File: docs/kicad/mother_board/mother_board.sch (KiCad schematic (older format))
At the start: 14 parts, among them J1 EXPR, J2 TFT_CONTROL, J3 TFT_DATA, J4 SERIAL, J5 LEDS, J6 ROTARY12, J7 ROTARY34, J8 SW_OUT, J9 SW_IN, U1 myTeensy3.6

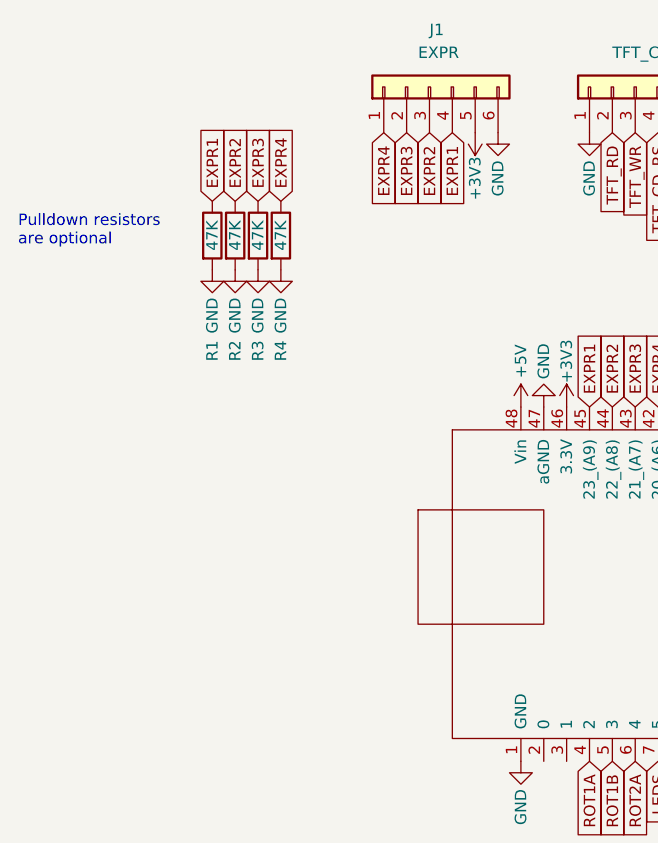
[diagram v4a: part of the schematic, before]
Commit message: added 1K resistor to pedal power to keep from crashing while inserting plugs
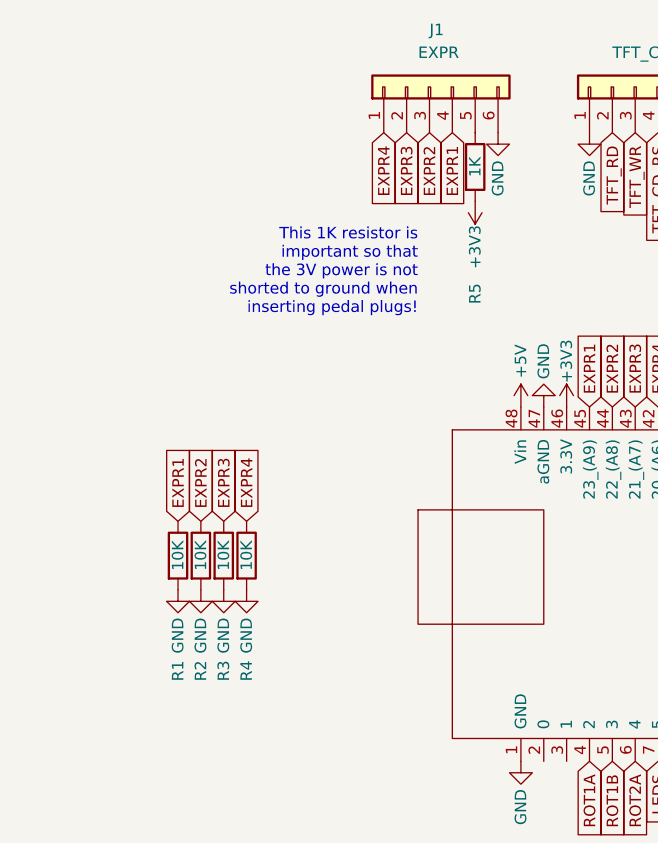
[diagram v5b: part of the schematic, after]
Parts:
- added R5: 1K, 0_my_footprints:myResistor, symbol Device:R
- R1, R2, R3, R4: value 47K -> 10K
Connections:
- net +3V3: now also R5.2; no longer J1.5 (Pin_5)
- new net: J1.5 (Pin_5), R5.1
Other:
- note added: "This 1K resistor is\nimportant so that\nthe 3V power is not \nshorted to ground when \ninserting pedal plugs!\n"
- note removed: "Pulldown resistors\nare optional"
- moved on the sheet: R1, R2, R3, R4
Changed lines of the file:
@@
 L power:+3V3 #PWR06
 U 1 1 64D07CE1
-P 4150 1500
-F 0 "#PWR06" H 4150 1350 50  0001 C CNN
-F 1 "+3V3" V 4150 1700 50  0000 C CNN
-F 2 "" H 4150 1500 50  0001 C CNN
-F 3 "" H 4150 1500 50  0001 C CNN
-	1    4150 1500
+P 4150 1800
+F 0 "#PWR06" H 4150 1650 50  0001 C CNN
+F 1 "+3V3" V 4150 2000 50  0000 C CNN
+F 2 "" H 4150 1800 50  0001 C CNN
+F 3 "" H 4150 1800 50  0001 C CNN
+	1    4150 1800
 	1    0    0    1
 $EndComp
-Text GLabel 3000 1800 1    50   Input ~ 0
+Text GLabel 2850 3200 1    50   Input ~ 0
 EXPR1
-Text GLabel 3100 1800 1    50   Input ~ 0
+Text GLabel 2950 3200 1    50   Input ~ 0
 EXPR2
-Text GLabel 3200 1800 1    50   Input ~ 0
+Text GLabel 3050 3200 1    50   Input ~ 0
 EXPR3
-Text GLabel 3300 1800 1    50   Input ~ 0
+Text GLabel 3150 3200 1    50   Input ~ 0
 EXPR4
 $Comp
 L Device:R R2
 U 1 1 64E4ADF9
-P 3100 1950
-F 0 "R2" V 3100 1400 50  0000 L CNN
-F 1 "47K" V 3100 1950 50  0000 C CNN
-F 2 "0_my_footprints:myResistor" V 3030 1950 50  0001 C CNN
-F 3 "~" H 3100 1950 50  0001 C CNN
-	1    3100 1950
+P 2950 3350
+F 0 "R2" V 2950 2800 50  0000 L CNN
+F 1 "10K" V 2950 3350 50  0000 C CNN
+F 2 "0_my_footprints:myResistor" V 2880 3350 50  0001 C CNN
+F 3 "~" H 2950 3350 50  0001 C CNN
+	1    2950 3350
 	1    0    0    -1
 $EndComp
@@
 L Device:R R3
 U 1 1 64E4B2A6
-P 3200 1950
-F 0 "R3" V 3200 1400 50  0000 L CNN
-F 1 "47K" V 3200 1950 50  0000 C CNN
-F 2 "0_my_footprints:myResistor" V 3130 1950 50  0001 C CNN
-F 3 "~" H 3200 1950 50  0001 C CNN
-	1    3200 1950
+P 3050 3350
+F 0 "R3" V 3050 2800 50  0000 L CNN
+F 1 "10K" V 3050 3350 50  0000 C CNN
+F 2 "0_my_footprints:myResistor" V 2980 3350 50  0001 C CNN
+F 3 "~" H 3050 3350 50  0001 C CNN
+	1    3050 3350
 	1    0    0    -1
 $EndComp
@@
 L Device:R R4
 U 1 1 64E4B7AB
-P 3300 1950
-F 0 "R4" V 3300 1400 50  0000 L CNN
-F 1 "47K" V 3300 1950 50  0000 C CNN
-F 2 "0_my_footprints:myResistor" V 3230 1950 50  0001 C CNN
-F 3 "~" H 3300 1950 50  0001 C CNN
-	1    3300 1950
+P 3150 3350
+F 0 "R4" V 3150 2800 50  0000 L CNN
+F 1 "10K" V 3150 3350 50  0000 C CNN
+F 2 "0_my_footprints:myResistor" V 3080 3350 50  0001 C CNN
+F 3 "~" H 3150 3350 50  0001 C CNN
+	1    3150 3350
 	1    0    0    -1
 $EndComp
@@
 L Device:R R1
 U 1 1 64CFCDE5
-P 3000 1950
-F 0 "R1" V 3000 1400 50  0000 L CNN
-F 1 "47K" V 3000 1950 50  0000 C CNN
-F 2 "0_my_footprints:myResistor" V 2930 1950 50  0001 C CNN
-F 3 "~" H 3000 1950 50  0001 C CNN
-	1    3000 1950
+P 2850 3350
+F 0 "R1" V 2850 2800 50  0000 L CNN
+F 1 "10K" V 2850 3350 50  0000 C CNN
+F 2 "0_my_footprints:myResistor" V 2780 3350 50  0001 C CNN
+F 3 "~" H 2850 3350 50  0001 C CNN
+	1    2850 3350
 	1    0    0    -1
 $EndComp
@@
 L power:GND #PWR0101
 U 1 1 64E50A7C
-P 3000 2100
-F 0 "#PWR0101" H 3000 1850 50  0001 C CNN
-F 1 "GND" V 3000 1900 50  0000 C CNN
-F 2 "" H 3000 2100 50  0001 C CNN
-F 3 "" H 3000 2100 50  0001 C CNN
-	1    3000 2100
+P 2850 3500
+F 0 "#PWR0101" H 2850 3250 50  0001 C CNN
+F 1 "GND" V 2850 3300 50  0000 C CNN
+F 2 "" H 2850 3500 50  0001 C CNN
+F 3 "" H 2850 3500 50  0001 C CNN
+	1    2850 3500
 	1    0    0    -1
 $EndComp
@@
 L power:GND #PWR0102
 U 1 1 64E50B86
-P 3100 2100
-F 0 "#PWR0102" H 3100 1850 50  0001 C CNN
-F 1 "GND" V 3100 1900 50  0000 C CNN
-F 2 "" H 3100 2100 50  0001 C CNN
-F 3 "" H 3100 2100 50  0001 C CNN
-	1    3100 2100
+P 2950 3500
+F 0 "#PWR0102" H 2950 3250 50  0001 C CNN
+F 1 "GND" V 2950 3300 50  0000 C CNN
+F 2 "" H 2950 3500 50  0001 C CNN
+F 3 "" H 2950 3500 50  0001 C CNN
+	1    2950 3500
 	1    0    0    -1
 $EndComp
@@
 L power:GND #PWR0103
 U 1 1 64E50E20
-P 3200 2100
-F 0 "#PWR0103" H 3200 1850 50  0001 C CNN
-F 1 "GND" V 3200 1900 50  0000 C CNN
-F 2 "" H 3200 2100 50  0001 C CNN
-F 3 "" H 3200 2100 50  0001 C CNN
-	1    3200 2100
+P 3050 3500
+F 0 "#PWR0103" H 3050 3250 50  0001 C CNN
+F 1 "GND" V 3050 3300 50  0000 C CNN
+F 2 "" H 3050 3500 50  0001 C CNN
+F 3 "" H 3050 3500 50  0001 C CNN
+	1    3050 3500
 	1    0    0    -1
 $EndComp
@@
 L power:GND #PWR0104
 U 1 1 64E50F3A
-P 3300 2100
-F 0 "#PWR0104" H 3300 1850 50  0001 C CNN
-F 1 "GND" V 3300 1900 50  0000 C CNN
-F 2 "" H 3300 2100 50  0001 C CNN
-F 3 "" H 3300 2100 50  0001 C CNN
-	1    3300 2100
+P 3150 3500
+F 0 "#PWR0104" H 3150 3250 50  0001 C CNN
+F 1 "GND" V 3150 3300 50  0000 C CNN
+F 2 "" H 3150 3500 50  0001 C CNN
+F 3 "" H 3150 3500 50  0001 C CNN
+	1    3150 3500
 	1    0    0    -1
 $EndComp
@@
 Text GLabel 4950 4250 3    50   Input ~ 0
 LEDS
-Text Notes 2150 2000 0    50   ~ 0
-Pulldown resistors\nare optional
+Text Notes 3900 2300 2    50   ~ 0
+This 1K resistor is\nimportant so that\nthe 3V power is not \nshorted to ground when \ninserting pedal plugs!\n
 $Bitmap
 Pos 5650 6600
@@
 Data
 89 50 4E 47 0D 0A 1A 0A 00 00 00 0D 49 48 44 52 00 00 00 E0 00 00 00 99 08 02 00 00 00 B9 62 A1
-BF 00 00 00 03 73 42 49 54 08 08 08 DB E1 4F E0 00 00 00 09 70 48 59 73 00 00 0B 12 00 00 0B 12
-01 D2 DD 7E FC 00 00 20 00 49 44 41 54 78 9C EC BD 79 BC 65 77 55 27 BA D6 FA 0D 7B 3A C3 3D F7
+BF 00 00 00 03 73 42 49 54 08 08 08 DB E1 4F E0 00 00 00 09 70 48 59 73 00 00 0A F0 00 00 0A F0
+01 42 AC 34 98 00 00 20 00 49 44 41 54 78 9C EC BD 79 BC 65 77 55 27 BA D6 FA 0D 7B 3A C3 3D F7
 DE BA B7 86 54 25 95 0A 09 64 02 81 E7 00 B6 08 22 88 A2 2D FD 01 69 C0 8F 82 A2 3C E1 D9 20 4E
 4F 1F 28 88 34 76 DB A0 A2 DD 62 4B 7F 68 DE 03 14 34 28 76 03 32 4A 0B 24 21 41 13 12 32 11 32
@@
 EndData
 $EndBitmap
+$Comp
+L Device:R R5
+U 1 1 64E70350
+P 4150 1650
+F 0 "R5" V 4150 1050 50  0000 L CNN
+F 1 "1K" V 4150 1650 50  0000 C CNN
+F 2 "0_my_footprints:myResistor" V 4080 1650 50  0001 C CNN
+F 3 "~" H 4150 1650 50  0001 C CNN
+	1    4150 1650
+	1    0    0    -1
+$EndComp
 $EndSCHEMATC

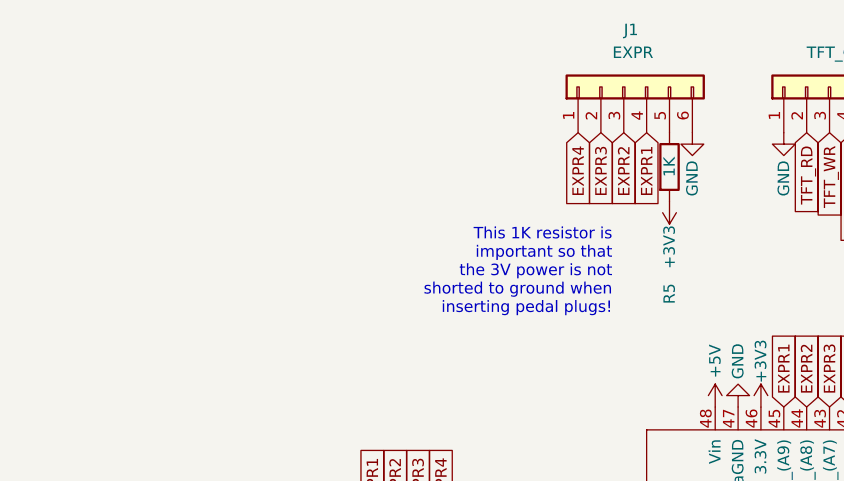
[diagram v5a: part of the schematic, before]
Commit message: notes regarding resistors for pedals
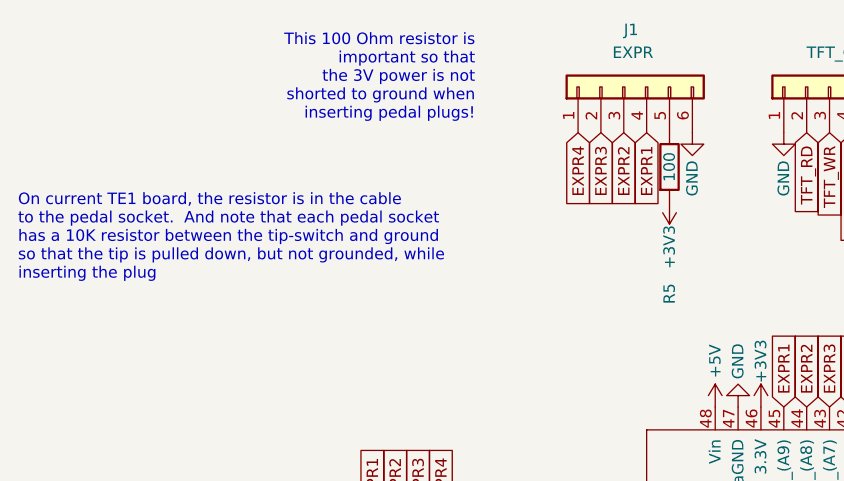
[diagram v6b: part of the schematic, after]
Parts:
- R5: value 1K -> 100
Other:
- note added: "On current TE1 board, the resistor is in the cable\nto the pedal socket. And note that each pedal socket\nhas a 10K resistor between the tip-switch and ground\nso that the tip is pulled down, but not grounded, while\ninserting the plug"
- note added: "This 100 Ohm resistor is\nimportant so that\nthe 3V power is not \nshorted to ground when \ninserting pedal plugs!\n"
- note removed: "This 1K resistor is\nimportant so that\nthe 3V power is not \nshorted to ground when \ninserting pedal plugs!\n"
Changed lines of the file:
@@
 Text GLabel 4950 4250 3    50   Input ~ 0
 LEDS
-Text Notes 3900 2300 2    50   ~ 0
-This 1K resistor is\nimportant so that\nthe 3V power is not \nshorted to ground when \ninserting pedal plugs!\n
+Text Notes 3300 1450 2    50   ~ 0
+This 100 Ohm resistor is\nimportant so that\nthe 3V power is not \nshorted to ground when \ninserting pedal plugs!\n
 $Bitmap
 Pos 5650 6600
@@
 P 4150 1650
 F 0 "R5" V 4150 1050 50  0000 L CNN
-F 1 "1K" V 4150 1650 50  0000 C CNN
+F 1 "100" V 4150 1650 50  0000 C CNN
 F 2 "0_my_footprints:myResistor" V 4080 1650 50  0001 C CNN
 F 3 "~" H 4150 1650 50  0001 C CNN
@@
 	1    0    0    -1
 $EndComp
+Text Notes 1300 2150 0    50   ~ 0
+On current TE1 board, the resistor is in the cable\nto the pedal socket.  And note that each pedal socket\nhas a 10K resistor between the tip-switch and ground\nso that the tip is pulled down, but not grounded, while\ninserting the plug
 $EndSCHEMATC
